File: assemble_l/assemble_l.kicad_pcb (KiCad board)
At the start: 2 copper layers, 128.5 x 102.6 mm, 51 parts, among them SW1 SW_Push, SW10 SW_Push, SW11 SW_Push, SW12 SW_Push, SW13 SW_Push, SW14 SW_Push, SW15 SW_Push, SW16 SW_Push, SW17 SW_Push, SW18 SW_Push, SW19 SW_Push, SW2 SW_Push, SW20 SW_Push, SW21 SW_Push, SW22 SW_Push, SW23 SW_SPDT, SW3 SW_Push, SW4 SW_Push, SW5 SW_Push, SW6 SW_Push, SW7 SW_Push, SW8 SW_Push, SW9 SW_Push, U1 Micon_BLEMicroPro

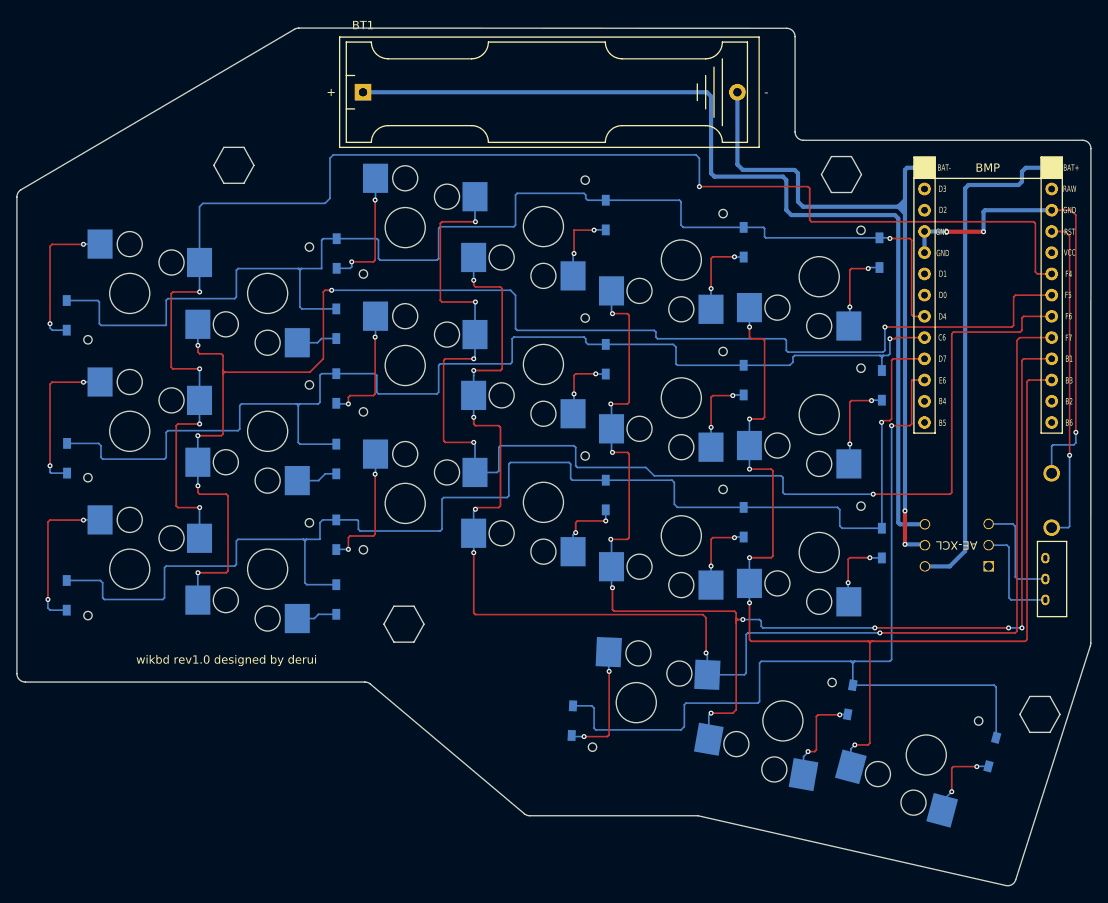
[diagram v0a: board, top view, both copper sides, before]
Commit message: feat: change PCB outline
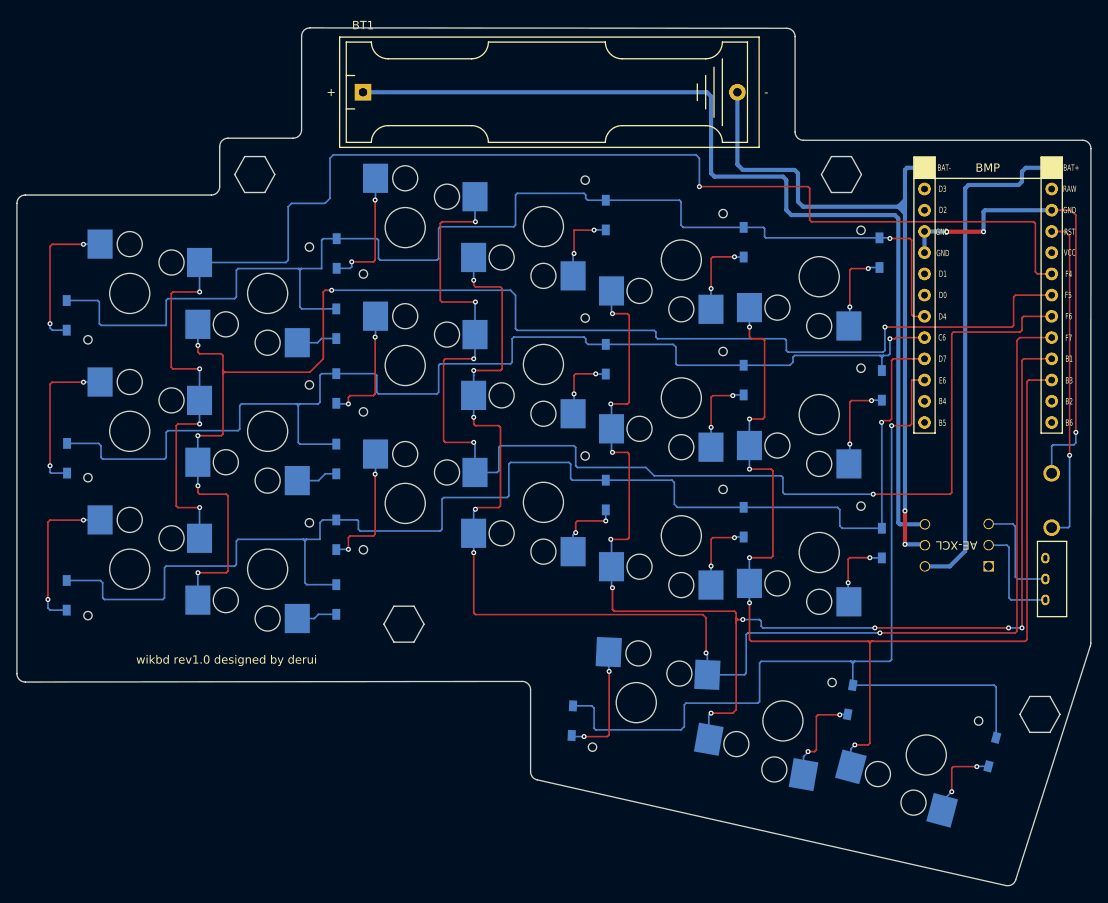
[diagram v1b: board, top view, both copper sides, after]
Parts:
- moved Ref** 2.73 mm to (85.0, 59.1)
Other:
- outline, holes or cut-outs redrawn
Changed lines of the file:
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@@
 		)
 		(fp_line
-			(start -1.999998 7.43)
+			(start -1.999997 7.43)
 			(end -2 3.4)
 			(stroke
@@
 	(footprint "kbd_Hole:m2_Spacer_Hole_hex"
 		(layer "F.Cu")
-		(at 82.5 58.05)
+		(at 85 59.15)
 		(descr "Mounting Hole 2.2mm, no annular, M2")
 		(tags "mounting hole 2.2mm no annular m2")
@@
 		)
 		(fp_line
-			(start 1.7 7.820002)
+			(start 1.7 7.820003)
 			(end 1.7 3.99)
 			(stroke
@@
 	)
 	(gr_arc
-		(start 56.5375 61.831232)
-		(mid 56.669716 61.334259)
-		(end 57.031443 60.968732)
+		(start 116.996217 119.803797)
+		(mid 117.705768 120.095347)
+		(end 118 120.80379)
 		(stroke
 			(width 0.05)
@@
 	)
 	(gr_line
-		(start 98.816668 120.110089)
-		(end 117.258332 135.639911)
+		(start 80.8 55.8)
+		(end 80.8 60.6)
+		(stroke
+			(width 0.05)
+			(type default)
+		)
+		(layer "Edge.Cuts")
+	)
+	(gr_arc
+		(start 90.6 42.600854)
+		(mid 90.893211 41.893475)
+		(end 91.600854 41.600855)
 		(stroke
 			(width 0.05)
@@
 	(gr_line
 		(start 174.875695 144.224991)
-		(end 138.0375 135.875)
+		(end 118.780031 131.575891)
+		(stroke
+			(width 0.05)
+			(type default)
+		)
+		(layer "Edge.Cuts")
+	)
+	(gr_arc
+		(start 118.780031 131.575891)
+		(mid 118.218985 131.224896)
+		(end 118 130.600384)
+		(stroke
+			(width 0.05)
+			(type default)
+		)
+		(layer "Edge.Cuts")
+	)
+	(gr_arc
+		(start 56.5375 62.6)
+		(mid 56.830393 61.892893)
+		(end 57.5375 61.6)
 		(stroke
 			(width 0.05)
@@
 	)
 	(gr_line
-		(start 89.765651 41.7625)
-		(end 57.031443 60.968732)
+		(start 89.6 54.8)
+		(end 81.8 54.8)
 		(stroke
 			(width 0.05)
@@
 	)
 	(gr_line
-		(start 56.5375 61.831232)
+		(start 56.5375 62.6)
 		(end 56.5375 118.875)
 		(stroke
@@
 		(layer "Edge.Cuts")
 	)
+	(gr_line
+		(start 57.5375 61.6)
+		(end 79.8 61.6)
+		(stroke
+			(width 0.05)
+			(type default)
+		)
+		(layer "Edge.Cuts")
+	)
 	(gr_arc
-		(start 98.172532 119.875)
-		(mid 98.515374 119.935619)
-		(end 98.816668 120.110089)
+		(start 80.8 60.6)
+		(mid 80.507107 61.307107)
+		(end 79.8 61.6)
 		(stroke
 			(width 0.05)
@@
 		(layer "Edge.Cuts")
 	)
-	(gr_line
-		(start 57.5375 119.875)
-		(end 98.172532 119.875)
+	(gr_arc
+		(start 80.8 55.8)
+		(mid 81.092893 55.092893)
+		(end 81.8 54.8)
 		(stroke
 			(width 0.05)
@@
 		(layer "Edge.Cuts")
 	)
-	(gr_arc
-		(start 89.765651 41.7625)
-		(mid 90.009506 41.659989)
-		(end 90.271708 41.625)
+	(gr_line
+		(start 116.996217 119.803797)
+		(end 57.5375 119.875)
 		(stroke
 			(width 0.05)
@@
 	(gr_line
 		(start 148.650421 41.649579)
-		(end 90.271708 41.625006)
-		(stroke
-			(width 0.05)
-			(type default)
-		)
-		(layer "Edge.Cuts")
-	)
-	(gr_arc
-		(start 117.902468 135.875)
-		(mid 117.559626 135.814381)
-		(end 117.258332 135.639911)
+		(end 91.600854 41.600855)
 		(stroke
 			(width 0.05)
@@
 		(layer "Edge.Cuts")
 	)
+	(gr_arc
+		(start 90.6 53.8)
+		(mid 90.307107 54.507107)
+		(end 89.6 54.8)
+		(stroke
+			(width 0.05)
+			(type default)
+		)
+		(layer "Edge.Cuts")
+	)
 	(gr_line
-		(start 138.0375 135.875)
-		(end 117.902468 135.875)
+		(start 90.6 42.600854)
+		(end 90.6 53.8)
 		(stroke
 			(width 0.05)
@@
 		(layer "Edge.Cuts")
 	)
+	(gr_line
+		(start 118 130.600384)
+		(end 118 120.80379)
+		(stroke
+			(width 0.05)
+			(type default)
+		)
+		(layer "Edge.Cuts")
+	)
 	(gr_arc
 		(start 148.650421 41.649579)
@@
 	)
 	(segment
-		(start 94 57.2)
-		(end 94 62)
+		(start 138.2 57.2)
+		(end 138.2 60.6)
 		(width 0.2)
 		(layer "B.Cu")
@@
 	)
 	(segment
-		(start 78.3875 72.9875)
-		(end 78.3875 69.675)
+		(start 94 62)
+		(end 94 57.2)
 		(width 0.2)
 		(layer "B.Cu")
@@
 	)
 	(segment
-		(start 137.8 56.8)
-		(end 94.4 56.8)
+		(start 78.3875 72.9875)
+		(end 78.3875 69.675)
 		(width 0.2)
 		(layer "B.Cu")
@@
 	)
 	(segment
-		(start 138.2 57.2)
-		(end 137.8 56.8)
+		(start 89 63)
+		(end 89.4 62.6)
 		(width 0.2)
 		(layer "B.Cu")
@@
 	)
 	(segment
-		(start 78.3875 63)
-		(end 78.3875 69.675)
+		(start 137.8 56.8)
+		(end 138.2 57.2)
 		(width 0.2)
 		(layer "B.Cu")
@@
 	)
 	(segment
-		(start 78.7875 62.6)
-		(end 78.3875 63)
+		(start 94 57.2)
+		(end 94.4 56.8)
 		(width 0.2)
 		(layer "B.Cu")
@@
 	)
 	(segment
-		(start 93.4 62.6)
-		(end 78.7875 62.6)
+		(start 89 69.4)
+		(end 89 63)
 		(width 0.2)
 		(layer "B.Cu")
@@
 	)
 	(segment
-		(start 94 62)
-		(end 93.4 62.6)
+		(start 78.3875 69.675)
+		(end 88.725 69.675)
 		(width 0.2)
 		(layer "B.Cu")
@@
 	)
 	(segment
-		(start 138.2 60.6)
-		(end 138.2 57.2)
+		(start 88.725 69.675)
+		(end 89 69.4)
 		(width 0.2)
 		(layer "B.Cu")
@@
 	(segment
 		(start 94.4 56.8)
-		(end 94 57.2)
+		(end 137.8 56.8)
+		(width 0.2)
+		(layer "B.Cu")
+		(net 29)
+	)
+	(segment
+		(start 89.4 62.6)
+		(end 93.4 62.6)
 		(width 0.2)
 		(layer "B.Cu")
@@
 		(width 0.2)
 		(layer "B.Cu")
+		(net 29)
+	)
+	(segment
+		(start 93.4 62.6)
+		(end 94 62)
+		(width 0.2)
+		(layer "B.Cu")

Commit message: feat: set prat settings
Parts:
- added Ref**: Val**, kbd_Hole:m2_Screw_Hole, F.Cu at (172.0, 109.4)
- added Ref**: Val**, kbd_Hole:m2_Screw_Hole, F.Cu at (165.3, 109.5)
- moved AE-XCL 2.00 mm to (169.0, 101.5)
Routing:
- net Bat-: track 84.9 -> 82.3 mm
- net Col2: track 145.8 -> 143.2 mm
- net Net-(BT1-+): track 117.5 -> 115.3 mm
- net Bat+: track 61.3 -> 59.1 mm
- net Net-(AE-XCL102D333CR-G1-EN): track 13.0 -> 14.9 mm
- net Net-(SW23-B): track 13.1 -> 14.8 mm
